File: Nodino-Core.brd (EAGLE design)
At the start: 27.9 x 25.4 mm, 15 parts, among them CON1 NODINO-JTAGMODULE, CON2 USB-OTG_SHIELD, IC1 STM32F373CCT6, IC3 AP733333SAG, Q1 16MHz, Y1 32.768kHz

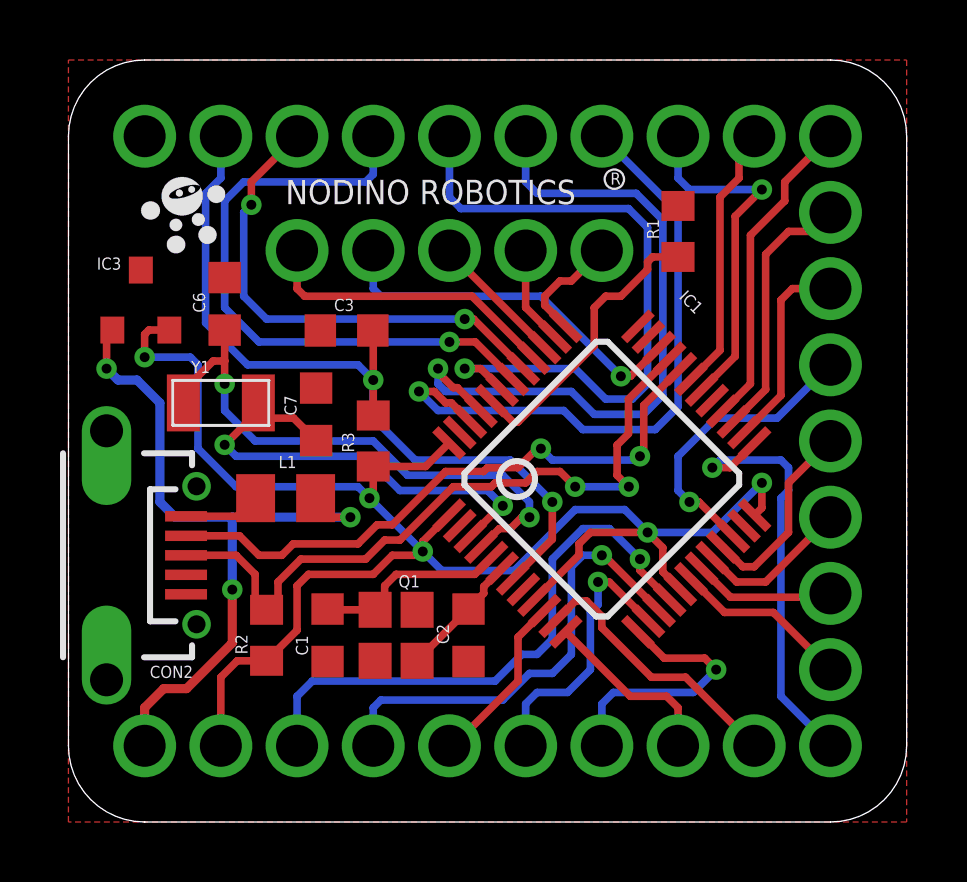
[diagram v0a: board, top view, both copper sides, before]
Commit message: Name and value renumbering
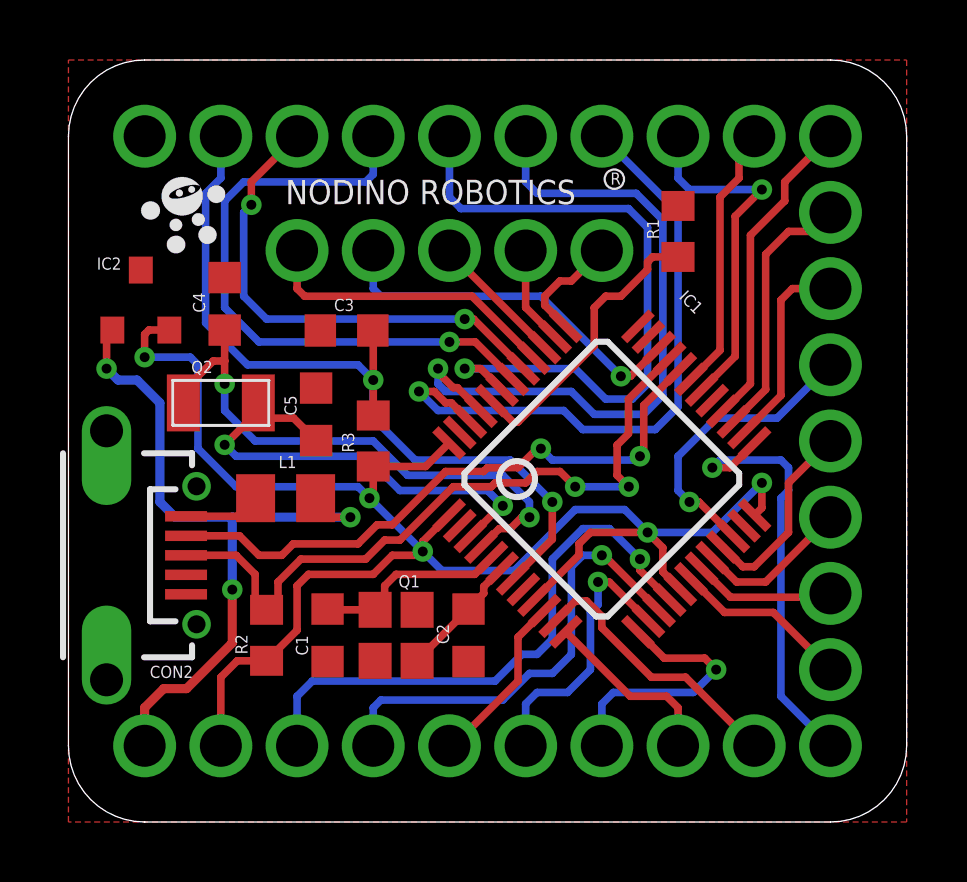
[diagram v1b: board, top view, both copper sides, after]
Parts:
- renumbered C6 to C4, C7 to C5, IC3 to IC2, Y1 to Q2
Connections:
- net CS1: now also CON1.3, IC1.16; no longer CON1.4, IC1.15
- net CS2: now also CON1.4, IC1.15; no longer CON1.3, IC1.16
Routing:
- net CS2: track 19.2 -> 15.4 mm
- net CS1: track 15.4 -> 19.2 mm
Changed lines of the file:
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@@
 <setting verticaltext="up"/>
 </settings>
-<grid distance="0.4" unitdist="mil" unit="mil" style="lines" multiple="1" display="yes" altdistance="0.025" altunitdist="inch" altunit="inch"/>
+<grid distance="0.005" unitdist="inch" unit="inch" style="lines" multiple="1" display="yes" altdistance="0.025" altunitdist="inch" altunit="inch"/>
 <layers>
 <layer number="1" name="Top" color="4" fill="1" visible="yes" active="yes"/>
@@
 <layer number="152" name="_bDocu" color="7" fill="1" visible="no" active="yes"/>
 <layer number="199" name="Contour" color="7" fill="1" visible="no" active="yes"/>
-<layer number="200" name="200bmp" color="1" fill="10" visible="yes" active="yes"/>
-<layer number="201" name="201bmp" color="2" fill="10" visible="yes" active="yes"/>
-<layer number="202" name="202bmp" color="3" fill="10" visible="yes" active="yes"/>
+<layer number="200" name="200bmp" color="1" fill="10" visible="no" active="yes"/>
+<layer number="201" name="201bmp" color="2" fill="10" visible="no" active="yes"/>
+<layer number="202" name="202bmp" color="3" fill="10" visible="no" active="yes"/>
 <layer number="203" name="203bmp" color="4" fill="10" visible="no" active="yes"/>
 <layer number="204" name="204bmp" color="5" fill="10" visible="no" active="yes"/>
@@
 <attribute name="VALUE" x="5.985" y="9.276" size="0.4064" layer="27"/>
 </element>
-<element name="C6" library="resistor" package="C0603K" value="22pF" x="5.207" y="17.272" smashed="yes" rot="R90">
+<element name="C4" library="resistor" package="C0603K" value="22pF" x="5.207" y="17.272" smashed="yes" rot="R90">
 <attribute name="NAME" x="4.557" y="16.98" size="0.4064" layer="25" rot="R90"/>
 <attribute name="VALUE" x="5.843" y="17.945" size="0.4064" layer="27" rot="R270"/>
 </element>
-<element name="C7" library="resistor" package="C0603K" value="22pF" x="8.255" y="13.589" smashed="yes" rot="R90">
+<element name="C5" library="resistor" package="C0603K" value="22pF" x="8.255" y="13.589" smashed="yes" rot="R90">
 <attribute name="NAME" x="7.605" y="13.551" size="0.4064" layer="25" rot="R90"/>
 <attribute name="VALUE" x="8.891" y="14.516" size="0.4064" layer="27" rot="R270"/>
 </element>
-<element name="Y1" library="abracon" package="ABS07" value="32.768kHz" x="5.08" y="13.97" smashed="yes">
+<element name="Q2" library="abracon" package="ABS07" value="32.768kHz" x="5.08" y="13.97" smashed="yes">
 <attribute name="NAME" x="4.092" y="14.966" size="0.4064" layer="25" font="vector" ratio="12"/>
 <attribute name="VALUE" x="6.58" y="13.049" size="0.4064" layer="27" font="vector" ratio="12" rot="R180"/>
 </element>
-<element name="IC3" library="diodes_inc" package="SOT23" value="AP733333SAG" x="2.413" y="17.399" smashed="yes">
+<element name="IC2" library="diodes_inc" package="SOT23" value="AP733333SAG" x="2.413" y="17.399" smashed="yes">
 <attribute name="NAME" x="0.944878125" y="18.40991875" size="0.4064" layer="25"/>
 <attribute name="VALUE" x="0.71628125" y="15.270478125" size="0.4064" layer="27" rot="R90"/>
@@
 <vertex x="0" y="0"/>
 </polygon>
-<contactref element="C6" pad="2"/>
-<contactref element="C7" pad="2"/>
-<contactref element="IC3" pad="3"/>
-<contactref element="IC3" pad="3"/>
+<contactref element="C4" pad="2"/>
+<contactref element="C5" pad="2"/>
+<contactref element="IC2" pad="3"/>
+<contactref element="IC2" pad="3"/>
 </signal>
 <signal name="+3V3">
@@
 <wire x1="10.16" y1="8.255" x2="10.795" y2="8.89" width="0.254" layer="1"/>
 <wire x1="10.795" y1="8.89" x2="11.684" y2="8.89" width="0.254" layer="1"/>
-<contactref element="IC3" pad="2"/>
+<contactref element="IC2" pad="2"/>
 <wire x1="23.114" y1="11.303" x2="21.463" y2="9.652" width="0.254" layer="16"/>
 <wire x1="21.463" y1="9.652" x2="19.304" y2="9.652" width="0.254" layer="16"/>
@@
 <wire x1="15.24" y1="3.937" x2="15.24" y2="2.54" width="0.254" layer="16"/>
 </signal>
-<signal name="CS1">
+<signal name="CS2">
 <contactref element="IC1" pad="15"/>
 <wire x1="19.6891875" y1="7.0459375" x2="17.845125" y2="8.89" width="0.254" layer="1"/>
@@
 <via x="21.59" y="5.08" extent="1-16" drill="0.3302"/>
 </signal>
-<signal name="CS2">
+<signal name="CS1">
 <contactref element="IC1" pad="16"/>
 <wire x1="20.042740625" y1="7.399490625" x2="19.05" y2="8.39223125" width="0.254" layer="1"/>
@@
 <wire x1="5.461" y1="10.16" x2="9.398" y2="10.16" width="0.3048" layer="16"/>
 <via x="9.398" y="10.16" extent="1-16" drill="0.3302"/>
-<contactref element="IC3" pad="1"/>
+<contactref element="IC2" pad="1"/>
 <wire x1="9.398" y1="10.16" x2="8.747" y2="10.16" width="0.254" layer="1"/>
 <wire x1="8.747" y1="10.16" x2="8.239" y2="10.795" width="0.254" layer="1"/>
@@
 </signal>
 <signal name="32K1">
-<contactref element="C6" pad="1"/>
+<contactref element="C4" pad="1"/>
 <contactref element="IC1" pad="4"/>
-<contactref element="Y1" pad="1"/>
+<contactref element="Q2" pad="1"/>
 <wire x1="13.749490625" y1="9.16725625" x2="14.361234375" y2="9.779" width="0.254" layer="1"/>
 <wire x1="14.361234375" y1="9.779" x2="14.732" y2="9.779" width="0.254" layer="1"/>
@@
 </signal>
 <signal name="32K2">
-<contactref element="C7" pad="1"/>
+<contactref element="C5" pad="1"/>
 <contactref element="IC1" pad="3"/>
-<contactref element="Y1" pad="2"/>
+<contactref element="Q2" pad="2"/>
 <via x="14.478" y="10.541" extent="1-16" drill="0.3302"/>
 <wire x1="14.478" y1="10.541" x2="14.416128125" y2="10.541" width="0.254" layer="1"/>
